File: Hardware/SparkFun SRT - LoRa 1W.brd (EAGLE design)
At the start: 50.8 x 27.9 mm, 73 parts, among them J1 QWIIC_RIGHT_ANGLE, J3 USB C, J4 JTAG, U2 ATSAMD21G-A, U3 AP2112K-3.3, U4 E19-915M30S, Y1 32.768kHz

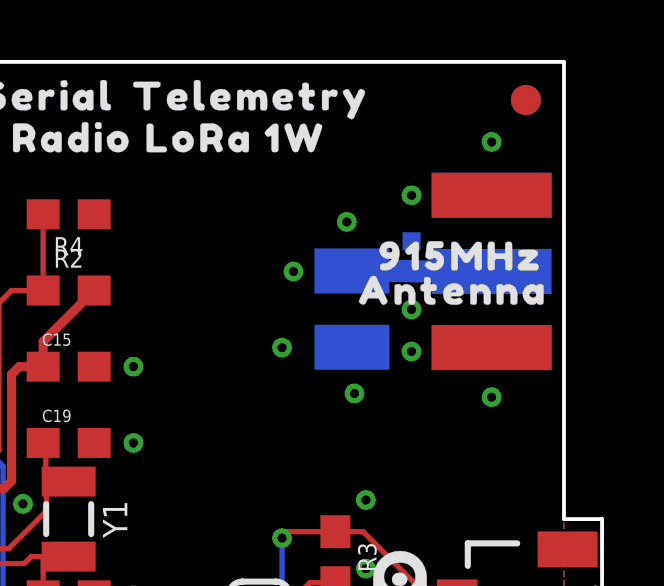
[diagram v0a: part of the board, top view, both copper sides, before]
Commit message: Add ignore. Fix RP-SMA connector.
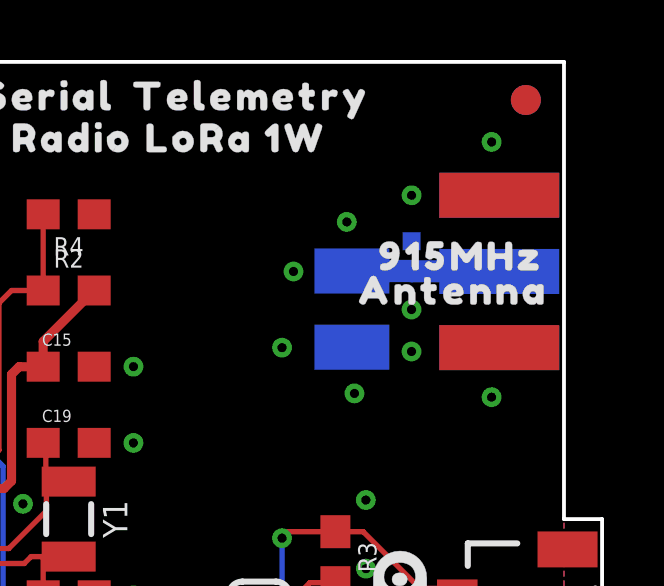
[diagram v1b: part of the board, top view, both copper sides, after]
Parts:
- removed E1: SMA, SparkFun-RF:SMA-EDGE
- added E2: RP-SMA, SparkFun-RF:SMA-EDGE
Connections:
- net GND: now also E2.GND@0, E2.GND@1, E2.GND@2, E2.GND@3; no longer E1.GND@0, E1.GND@1, E1.GND@2, E1.GND@3
- net LORA_ANT: now also E2.SIG; no longer E1.SIG
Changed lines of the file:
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@@
 <layer number="23" name="tOrigins" color="15" fill="1" visible="yes" active="yes"/>
 <layer number="24" name="bOrigins" color="15" fill="1" visible="yes" active="yes"/>
-<layer number="25" name="tNames" color="7" fill="1" visible="no" active="yes"/>
-<layer number="26" name="bNames" color="7" fill="1" visible="no" active="yes"/>
-<layer number="27" name="tValues" color="7" fill="1" visible="no" active="yes"/>
-<layer number="28" name="bValues" color="7" fill="1" visible="no" active="yes"/>
-<layer number="29" name="tStop" color="7" fill="3" visible="no" active="yes"/>
-<layer number="30" name="bStop" color="7" fill="6" visible="no" active="yes"/>
-<layer number="31" name="tCream" color="7" fill="4" visible="no" active="yes"/>
-<layer number="32" name="bCream" color="7" fill="5" visible="no" active="yes"/>
-<layer number="33" name="tFinish" color="6" fill="3" visible="no" active="yes"/>
-<layer number="34" name="bFinish" color="6" fill="6" visible="no" active="yes"/>
-<layer number="35" name="tGlue" color="7" fill="4" visible="no" active="yes"/>
-<layer number="36" name="bGlue" color="7" fill="5" visible="no" active="yes"/>
-<layer number="37" name="tTest" color="7" fill="1" visible="no" active="yes"/>
-<layer number="38" name="bTest" color="7" fill="1" visible="no" active="yes"/>
-<layer number="39" name="tKeepout" color="4" fill="11" visible="no" active="yes"/>
-<layer number="40" name="bKeepout" color="1" fill="11" visible="no" active="yes"/>
-<layer number="41" name="tRestrict" color="4" fill="10" visible="no" active="yes"/>
-<layer number="42" name="bRestrict" color="1" fill="10" visible="no" active="yes"/>
-<layer number="43" name="vRestrict" color="2" fill="10" visible="no" active="yes"/>
-<layer number="44" name="Drills" color="7" fill="1" visible="no" active="yes"/>
+<layer number="25" name="tNames" color="7" fill="1" visible="yes" active="yes"/>
+<layer number="26" name="bNames" color="7" fill="1" visible="yes" active="yes"/>
+<layer number="27" name="tValues" color="7" fill="1" visible="yes" active="yes"/>
+<layer number="28" name="bValues" color="7" fill="1" visible="yes" active="yes"/>
+<layer number="29" name="tStop" color="7" fill="3" visible="yes" active="yes"/>
+<layer number="30" name="bStop" color="7" fill="6" visible="yes" active="yes"/>
+<layer number="31" name="tCream" color="7" fill="4" visible="yes" active="yes"/>
+<layer number="32" name="bCream" color="7" fill="5" visible="yes" active="yes"/>
+<layer number="33" name="tFinish" color="6" fill="3" visible="yes" active="yes"/>
+<layer number="34" name="bFinish" color="6" fill="6" visible="yes" active="yes"/>
+<layer number="35" name="tGlue" color="7" fill="4" visible="yes" active="yes"/>
+<layer number="36" name="bGlue" color="7" fill="5" visible="yes" active="yes"/>
+<layer number="37" name="tTest" color="7" fill="1" visible="yes" active="yes"/>
+<layer number="38" name="bTest" color="7" fill="1" visible="yes" active="yes"/>
+<layer number="39" name="tKeepout" color="4" fill="11" visible="yes" active="yes"/>
+<layer number="40" name="bKeepout" color="1" fill="11" visible="yes" active="yes"/>
+<layer number="41" name="tRestrict" color="4" fill="10" visible="yes" active="yes"/>
+<layer number="42" name="bRestrict" color="1" fill="10" visible="yes" active="yes"/>
+<layer number="43" name="vRestrict" color="2" fill="10" visible="yes" active="yes"/>
+<layer number="44" name="Drills" color="7" fill="1" visible="yes" active="yes"/>
 <layer number="45" name="Holes" color="7" fill="1" visible="yes" active="yes"/>
-<layer number="46" name="Milling" color="3" fill="1" visible="no" active="yes"/>
-<layer number="47" name="Measures" color="7" fill="1" visible="no" active="yes"/>
-<layer number="48" name="Document" color="7" fill="1" visible="no" active="yes"/>
+<layer number="46" name="Milling" color="3" fill="1" visible="yes" active="yes"/>
+<layer number="47" name="Measures" color="7" fill="1" visible="yes" active="yes"/>
+<layer number="48" name="Document" color="7" fill="1" visible="yes" active="yes"/>
 <layer number="49" name="Reference" color="7" fill="1" visible="yes" active="yes"/>
-<layer number="50" name="dxf" color="7" fill="1" visible="no" active="yes"/>
+<layer number="50" name="dxf" color="7" fill="1" visible="yes" active="yes"/>
 <layer number="51" name="tDocu" color="6" fill="1" visible="yes" active="yes"/>
-<layer number="52" name="bDocu" color="7" fill="1" visible="no" active="yes"/>
+<layer number="52" name="bDocu" color="7" fill="1" visible="yes" active="yes"/>
 <layer number="2" name="Route2" color="63" fill="3" visible="no" active="no"/>
 <layer number="15" name="Route15" color="23" fill="6" visible="no" active="no"/>
@@
 <attribute name="VALUE" x="3.937" y="25.4" size="0.6096" layer="27" font="vector" ratio="20" rot="R270" align="top-center"/>
 </element>
-<element name="E1" library="SparkFun-RF" package="SMA-EDGE" value="SMA" x="47.117" y="20.955" smashed="yes" rot="MR90">
-<attribute name="PROD_ID" value="CONN-08289" x="47.117" y="20.955" size="1.778" layer="28" font="vector" ratio="15" rot="MR90" display="off"/>
-</element>
 <element name="U$1" library="output" package="SERIAL0" value="" x="32.385" y="26.797" smashed="yes"/>
 <element name="U$4" library="output" package="TELEMETRY1" value="" x="39.116" y="26.797" smashed="yes"/>
@@
 <element name="U$16" library="output" package="C0" value="" x="6.223" y="8.255" smashed="yes" rot="R90"/>
 <element name="U$17" library="output" package="R1" value="" x="6.223" y="9.525" smashed="yes" rot="R90"/>
+<element name="E2" library="SparkFun-RF" package="SMA-EDGE" value="RP-SMA" x="47.371" y="20.955" smashed="yes" rot="MR90">
+<attribute name="PROD_ID" value="CONN-00827" x="47.371" y="20.955" size="1.778" layer="28" font="vector" ratio="15" rot="MR90" display="off"/>
+</element>
 </elements>
 <signals>
@@
 <contactref element="R7" pad="1"/>
 <contactref element="R8" pad="1"/>
-<contactref element="E1" pad="GND@1"/>
-<contactref element="E1" pad="GND@2"/>
-<contactref element="E1" pad="GND@3"/>
-<contactref element="E1" pad="GND@0"/>
 <contactref element="J2" pad="1"/>
 <contactref element="R1" pad="1"/>
@@
 <via x="4.953" y="27.178" extent="1-16" drill="0.3048"/>
 <via x="5.08" y="23.876" extent="1-16" drill="0.3048"/>
+<contactref element="E2" pad="GND@3"/>
+<contactref element="E2" pad="GND@2"/>
+<contactref element="E2" pad="GND@0"/>
+<contactref element="E2" pad="GND@1"/>
 </signal>
 <signal name="3.3V" class="1">
@@
 <signal name="LORA_ANT">
 <contactref element="U4" pad="19"/>
-<contactref element="E1" pad="SIG"/>
 <contactref element="D6" pad="2"/>
-<wire x1="44.443" y1="20.97" x2="42.46" y2="20.97" width="0.739140625" layer="16"/>
-<wire x1="44.45" y1="20.963" x2="47.109" y2="20.963" width="0.739140625" layer="16"/>
-<wire x1="47.109" y1="20.963" x2="47.117" y2="20.955" width="0.739140625" layer="16"/>
-<wire x1="44.45" y1="20.963" x2="44.443" y2="20.97" width="0.739140625" layer="16"/>
+<contactref element="E2" pad="SIG"/>
+<wire x1="42.46" y1="20.97" x2="44.443" y2="20.97" width="0.739140625" layer="16"/>
+<wire x1="44.443" y1="20.97" x2="44.45" y2="20.963" width="0.739140625" layer="16"/>
+<wire x1="44.45" y1="20.963" x2="47.363" y2="20.963" width="0.739140625" layer="16"/>
+<wire x1="47.363" y1="20.963" x2="47.371" y2="20.955" width="0.739140625" layer="16"/>
 </signal>
 <signal name="RTS-O">

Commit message: Update to new RP SMA connector package
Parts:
- E2: device SparkFun-RF:SMA-EDGE -> SparkFun-RF:RP-SMA-EDGE
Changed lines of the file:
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@@
 HASL RoHS Finish</text>
 <text x="122.99" y="-9.26" size="1.778" layer="51" ratio="15">N. Seidle</text>
-<dimension x1="0" y1="0" x2="59" y2="0" x3="29.5" y3="-7" textsize="1.778" textratio="15" layer="47" dtype="horizontal"/>
-<dimension x1="0" y1="0" x2="0" y2="34" x3="-4" y3="17" textsize="1.778" textratio="15" layer="47" dtype="vertical"/>
+<dimension x1="0" y1="0" x2="49.53" y2="-1.27" x3="24.765" y3="-7" textsize="1.778" textratio="15" layer="47" dtype="horizontal"/>
+<dimension x1="0" y1="0" x2="0" y2="27.94" x3="-4" y3="13.97" textsize="1.778" textratio="15" layer="47" dtype="vertical"/>
 <text x="30" y="-9" size="1.778" layer="47" font="vector" ratio="15" align="center">Dimensions in mm</text>
 <wire x1="1.27" y1="27.94" x2="49.53" y2="27.94" width="0.127" layer="20"/>
@@
 <element name="U$16" library="output" package="C0" value="" x="6.223" y="8.255" smashed="yes" rot="R90"/>
 <element name="U$17" library="output" package="R1" value="" x="6.223" y="9.525" smashed="yes" rot="R90"/>
-<element name="E2" library="SparkFun-RF" package="SMA-EDGE" value="RP-SMA" x="47.371" y="20.955" smashed="yes" rot="MR90">
+<element name="E2" library="SparkFun-RF" package="RP-SMA-EDGE" value="RP-SMA" x="47.371" y="20.955" smashed="yes" rot="MR90">
 <attribute name="PROD_ID" value="CONN-00827" x="47.371" y="20.955" size="1.778" layer="28" font="vector" ratio="15" rot="MR90" display="off"/>
 </element>
